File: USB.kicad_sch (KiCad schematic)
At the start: 91 parts, among them J1 USB_A, J2 USB-C Receptacle, J3 USB_A, J4 USB_A, J5 USB_A, U3 GL3523-OTY30, U4 USB-PD, U5 LPW5209AB5F, U6 LPW5209AB5F, U7 LPW5209AB5F, U8 LPW5209AB5F, U9 W25Q128JVS, Y1 Crystal 25MHz 2016

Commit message: initial routing
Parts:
- added C43: Cap 4.7uF 0402, Capacitor_SMD:C_0402_1005Metric, symbol Kalid:Cap 4.7uF 0402
- J1, J3, J4, J5: footprint Connector_USB:USB_A_Connfly_DS1095 -> Kalid:USB_A_Connfly_DS1095; LCSC (none) -> C456018; MPN (none) -> AF 90° WJDG; Manufacturer (none) -> SHOU HAN(首韩)
- J2: footprint Connector_USB:USB_C_Receptacle_HRO_TYPE-C-31-M-12 -> Kalid:USB_C_Receptacle_HRO_TYPE-C-31-M-12
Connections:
- net +1.2V: now also C21.1, C43.1
- net +V5V: no longer C21.1
- net GND: now also C43.2
- net USB_UFP_D+: no longer R42.2
- net USB_UFP_D-: no longer R43.2
- net P3_D-: now reaches J4.2 (D-), U3.14 (DM_P3)
- net P3_D+: now reaches J4.3 (D+), U3.13 (DP_P3)
- net at R40.1, U4.4 (D+): now also R43.1
- net at R41.1, U4.5 (D-): now also R42.1
- net P2_D+: now reaches J3.3 (D+), U3.25 (DP_P2)
- net P2_D-: now reaches J3.2 (D-), U3.26 (DM_P2)
- net P1_D-: now reaches J1.2 (D-), U3.64 (DM_P1)
- net P1_D+: now reaches J1.3 (D+), U3.63 (DP_P1)
- net P4_D+: now reaches J5.3 (D+), U3.10 (DP_P4)
- net P4_D-: now reaches J5.2 (D-), U3.11 (DM_P4)

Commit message: finish routing
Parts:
- added C44: Cap 4.7uF 0402, Capacitor_SMD:C_0402_1005Metric, symbol Kalid:Cap 4.7uF 0402
- added H1, H2, H3, H4: Mounting Hole, MountingHole:MountingHole_2.2mm_M2_DIN965_Pad_TopOnly, symbol Mechanical:MountingHole_Pad
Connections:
- net +1.2V: now also C44.1
- net +V5V: no longer C32.1, U4.2 (VUSB)
- net +VUSBIN: now also C32.1, U4.2 (VUSB)
- net GND: now also C44.2, H1.1, H2.1, H3.1, H4.1

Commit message: name the project
Signed-off-by: Sean Cross <sean@xobs.io>
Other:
- title: (none) -> Kalid
- moved on the sheet: H1, H2, H3, H4
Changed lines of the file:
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@@
 	(generator_version "9.0")
 	(paper "A4")
+	(title_block
+		(title "Kalid")
+		(date "2025-07-28")
+		(rev "EVT1")
+	)
 	(rectangle
 		(start 20.32 156.21)
@@
 	(symbol
 		(lib_id "Mechanical:MountingHole_Pad")
-		(at 142.24 106.68 0)
+		(at 130.81 85.09 0)
 		(unit 1)
 		(exclude_from_sim no)
@@
 		(fields_autoplaced yes)
 		(property "Reference" "H2"
-			(at 144.78 104.1399 0)
+			(at 133.35 82.5499 0)
 			(effects
 				(font
@@
 		)
 		(property "Value" "Mounting Hole"
-			(at 144.78 106.6799 0)
+			(at 133.35 85.0899 0)
 			(effects
 				(font
@@
 		)
 		(property "Footprint" "MountingHole:MountingHole_2.2mm_M2_DIN965_Pad_TopOnly"
-			(at 142.24 106.68 0)
+			(at 130.81 85.09 0)
 			(effects
 				(font
@@
 		)
 		(property "Datasheet" "~"
-			(at 142.24 106.68 0)
+			(at 130.81 85.09 0)
 			(effects
 				(font
@@
 		)
 		(property "Description" "Mounting Hole with connection"
-			(at 142.24 106.68 0)
+			(at 130.81 85.09 0)
 			(effects
 				(font
@@
 	(symbol
 		(lib_id "power:GND")
-		(at 121.92 109.22 0)
+		(at 110.49 87.63 0)
 		(unit 1)
 		(exclude_from_sim no)
@@
 		(fields_autoplaced yes)
 		(property "Reference" "#PWR086"
-			(at 121.92 115.57 0)
+			(at 110.49 93.98 0)
 			(effects
 				(font
@@
 		)
 		(property "Value" "GND"
-			(at 121.92 114.3 0)
+			(at 110.49 92.71 0)
 			(effects
 				(font
@@
 		)
 		(property "Footprint" ""
-			(at 121.92 109.22 0)
+			(at 110.49 87.63 0)
 			(effects
 				(font
@@
 		)
 		(property "Datasheet" ""
-			(at 121.92 109.22 0)
+			(at 110.49 87.63 0)
 			(effects
 				(font
@@
 		)
 		(property "Description" ""
-			(at 121.92 109.22 0)
+			(at 110.49 87.63 0)
 			(effects
 				(font
@@
 	(symbol
 		(lib_id "Mechanical:MountingHole_Pad")
-		(at 121.92 118.11 0)
+		(at 110.49 96.52 0)
 		(unit 1)
 		(exclude_from_sim no)
@@
 		(fields_autoplaced yes)
 		(property "Reference" "H3"
-			(at 124.46 115.5699 0)
+			(at 113.03 93.9799 0)
 			(effects
 				(font
@@
 		)
 		(property "Value" "Mounting Hole"
-			(at 124.46 118.1099 0)
+			(at 113.03 96.5199 0)
 			(effects
 				(font
@@
 		)
 		(property "Footprint" "MountingHole:MountingHole_2.2mm_M2_DIN965_Pad_TopOnly"
-			(at 121.92 118.11 0)
+			(at 110.49 96.52 0)
 			(effects
 				(font
@@
 		)
 		(property "Datasheet" "~"
-			(at 121.92 118.11 0)
+			(at 110.49 96.52 0)
 			(effects
 				(font
@@
 		)
 		(property "Description" "Mounting Hole with connection"
-			(at 121.92 118.11 0)
+			(at 110.49 96.52 0)
 			(effects
 				(font
@@
 	(symbol
 		(lib_id "Mechanical:MountingHole_Pad")
-		(at 142.24 118.11 0)
+		(at 130.81 96.52 0)
 		(unit 1)
 		(exclude_from_sim no)
@@
 		(fields_autoplaced yes)
 		(property "Reference" "H4"
-			(at 144.78 115.5699 0)
+			(at 133.35 93.9799 0)
 			(effects
 				(font
@@
 		)
 		(property "Value" "Mounting Hole"
-			(at 144.78 118.1099 0)
+			(at 133.35 96.5199 0)
 			(effects
 				(font
@@
 		)
 		(property "Footprint" "MountingHole:MountingHole_2.2mm_M2_DIN965_Pad_TopOnly"
-			(at 142.24 118.11 0)
+			(at 130.81 96.52 0)
 			(effects
 				(font
@@
 		)
 		(property "Datasheet" "~"
-			(at 142.24 118.11 0)
+			(at 130.81 96.52 0)
 			(effects
 				(font
@@
 		)
 		(property "Description" "Mounting Hole with connection"
-			(at 142.24 118.11 0)
+			(at 130.81 96.52 0)
 			(effects
 				(font
@@
 	(symbol
 		(lib_id "Mechanical:MountingHole_Pad")
-		(at 121.92 106.68 0)
+		(at 110.49 85.09 0)
 		(unit 1)
 		(exclude_from_sim no)
@@
 		(fields_autoplaced yes)
 		(property "Reference" "H1"
-			(at 124.46 104.1399 0)
+			(at 113.03 82.5499 0)
 			(effects
 				(font
@@
 		)
 		(property "Value" "Mounting Hole"
-			(at 124.46 106.6799 0)
+			(at 113.03 85.0899 0)
 			(effects
 				(font
@@
 		)
 		(property "Footprint" "MountingHole:MountingHole_2.2mm_M2_DIN965_Pad_TopOnly"
-			(at 121.92 106.68 0)
+			(at 110.49 85.09 0)
 			(effects
 				(font
@@
 		)
 		(property "Datasheet" "~"
-			(at 121.92 106.68 0)
+			(at 110.49 85.09 0)
 			(effects
 				(font
@@
 		)
 		(property "Description" "Mounting Hole with connection"
-			(at 121.92 106.68 0)
+			(at 110.49 85.09 0)
 			(effects
 				(font
@@
 	(symbol
 		(lib_id "power:GND")
-		(at 142.24 120.65 0)
+		(at 130.81 99.06 0)
 		(unit 1)
 		(exclude_from_sim no)
@@
 		(fields_autoplaced yes)
 		(property "Reference" "#PWR089"
-			(at 142.24 127 0)
+			(at 130.81 105.41 0)
 			(effects
 				(font
@@
 		)
 		(property "Value" "GND"
-			(at 142.24 125.73 0)
+			(at 130.81 104.14 0)
 			(effects
 				(font
@@
 		)
 		(property "Footprint" ""
-			(at 142.24 120.65 0)
+			(at 130.81 99.06 0)
 			(effects
 				(font
@@
 		)
 		(property "Datasheet" ""
-			(at 142.24 120.65 0)
+			(at 130.81 99.06 0)
 			(effects
 				(font
@@
 		)
 		(property "Description" ""
-			(at 142.24 120.65 0)
+			(at 130.81 99.06 0)
 			(effects
 				(font
@@
 	(symbol
 		(lib_id "power:GND")
-		(at 121.92 120.65 0)
+		(at 110.49 99.06 0)
 		(unit 1)
 		(exclude_from_sim no)
@@
 		(fields_autoplaced yes)
 		(property "Reference" "#PWR088"
-			(at 121.92 127 0)
+			(at 110.49 105.41 0)
 			(effects
 				(font
@@
 		)
 		(property "Value" "GND"
-			(at 121.92 125.73 0)
+			(at 110.49 104.14 0)
 			(effects
 				(font
@@
 		)
 		(property "Footprint" ""
-			(at 121.92 120.65 0)
+			(at 110.49 99.06 0)
 			(effects
 				(font
@@
 		)
 		(property "Datasheet" ""
-			(at 121.92 120.65 0)
+			(at 110.49 99.06 0)
 			(effects
 				(font
@@
 		)
 		(property "Description" ""
-			(at 121.92 120.65 0)
+			(at 110.49 99.06 0)
 			(effects
 				(font
@@
 	(symbol
 		(lib_id "power:GND")
-		(at 142.24 109.22 0)
+		(at 130.81 87.63 0)
 		(unit 1)
 		(exclude_from_sim no)
@@
 		(fields_autoplaced yes)
 		(property "Reference" "#PWR087"
-			(at 142.24 115.57 0)
+			(at 130.81 93.98 0)
 			(effects
 				(font
@@
 		)
 		(property "Value" "GND"
-			(at 142.24 114.3 0)
+			(at 130.81 92.71 0)
 			(effects
 				(font
@@
 		)
 		(property "Footprint" ""
-			(at 142.24 109.22 0)
+			(at 130.81 87.63 0)
 			(effects
 				(font
@@
 		)
 		(property "Datasheet" ""
-			(at 142.24 109.22 0)
+			(at 130.81 87.63 0)
 			(effects
 				(font
@@
 		)
 		(property "Description" ""
-			(at 142.24 109.22 0)
+			(at 130.81 87.63 0)
 			(effects
 				(font

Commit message: develop evt2
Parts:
- removed C17: Cap 4.7uF 0402, Capacitor_SMD:C_0402_1005Metric, symbol Kalid:Cap 4.7uF 0402
- removed L3: 10uH, 4.5A, Inductor_SMD:L_Changjiang_FXL0630, symbol Device:L
- removed R14, R15, R36: R 10k 0402, Resistor_SMD:R_0402_1005Metric, symbol Kalid:R 10k 0402
- removed R44, R45: R 0 ohm 0402, Resistor_SMD:R_0402_1005Metric, symbol Kalid:R 0 ohm 0402
- added L3: L 2.2uH 2A, Kalid:IND-SMD_L3.0-W3.0_LQH3NPN, symbol Kalid:L 2.2uH 2A
- added R14, R15: R 0 ohm 0402, Resistor_SMD:R_0402_1005Metric, symbol Kalid:R 0 ohm 0402
- added R36: R 5.1k 0402, Resistor_SMD:R_0402_1005Metric, symbol Kalid:R 5.1k 0402
- R39: now not fitted; now left out of the parts list
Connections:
- net +3.3V: now also R37.2, R38.2, R39.2, R14.2
- net +V5V: now also R15.2; no longer U3.54 (VBUS)
- net GND: now also R13.2; no longer R39.1
- net at U3.41 (SW): now also L3.2
- net at U3.45 (CHIPEN): now also R14.1, R15.1
- net at R38.1: now also U9.7 (~{HOLD}/~{RESET}/IO_{3}); no longer R39.2
- net at R12.1, U3.48 (RESETJ): now also R39.1; no longer R13.1
- net SPI_CS: now reaches U3.52 (P_SPI_CZ), U9.1 (~{CS})
- net SPI_CIPO: now reaches U9.2 (DO/IO_{1})
- net SPI_CIPO: now also U3.51 (P_SPI_DI); no longer U3.49 (P_SPI_DO)
- net at U9.3 (~{WP}/IO_{2}): now also R37.1
- net SPI_COPI: now reaches U9.5 (DI/IO_{0})
- net SPI_COPI: now also U3.49 (P_SPI_DO); no longer U3.51 (P_SPI_DI)
- net SPI_CLK: now reaches U3.50 (P_SPI_CK), U9.6 (CLK)
- net at R21.1: now also L3.1
- new net: R13.1, R36.1, U3.54 (VBUS)
- new net +V5VUSB: R36.2
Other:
- note removed: "10k on top, 50k on the bottom"
- moved on the sheet: C20, R12, R13

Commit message: evt3
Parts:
- removed C44: Cap 4.7uF 0402, Capacitor_SMD:C_0402_1005Metric, symbol Kalid:Cap 4.7uF 0402
- added C17: Cap 12pF 0402, Capacitor_SMD:C_0402_1005Metric, symbol Kalid:Cap 12pF 0402
- added FB1: 120 ohm, Inductor_SMD:L_0402_1005Metric, symbol Device:FerriteBead_Small
- added J6: Conn_01x04, Connector_PinSocket_2.54mm:PinSocket_1x04_P2.54mm_Vertical, symbol Connector_Generic:Conn_01x04
- added R44, R45, R58, R59, R60, R61, R62, R63: R 10k 0402, Resistor_SMD:R_0402_1005Metric, symbol Kalid:R 10k 0402
- added R64: R 0 ohm 0402, Resistor_SMD:R_0402_1005Metric, symbol Kalid:R 0 ohm 0402
- added TP11, TP8, TP9: TestPoint, TestPoint:TestPoint_Pad_D1.5mm, symbol Connector:TestPoint
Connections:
- net +1.2V: now also L3.1, R21.1, C17.2, FB1.1, TP9.1; no longer C27.1, C28.1, C30.1, C31.1, C38.1, R21.2, R22.1, U3.17 (VP12_P3), U3.22 (VP12_P2), U3.39 (FB), U3.60 (VP12_P1), U3.7 (VP12_P4), U3.70 (VP12_P0)
- net +3.3V: now also TP8.1
- net +V5V: now also R45.1, R59.1, R61.1, R63.1
- net GND: now also J6.1 (Pin_1), R44.2, R58.2, R60.2, R62.2, R64.2
- net SPI_CIPO: now also U3.49 (P_SPI_DO); no longer U3.51 (P_SPI_DI)
- net SPI_COPI: now also U3.51 (P_SPI_DI); no longer U3.49 (P_SPI_DO)
- net at TP4.1, U3.35 (OVCUR2J): now also R58.1, R59.2
- net SMD: now reaches TP6.1, U3.31 (OVCUR4J/SMD)
- net SMD: now also J6.3 (Pin_3), R62.1, R63.2
- net SMC: now reaches TP5.1, U3.34 (OVCUR3J/SMC)
- net SMC: now also J6.2 (Pin_2), R60.1, R61.2
- net RESETJ: now reaches R12.1, R39.1, U3.48 (RESETJ)
- net RESETJ: now also J6.4 (Pin_4), R64.1
- net at TP3.1, U3.38 (OVCUR1J): now also R44.1, R45.2
- new net: C17.1, R21.2, R22.1, U3.39 (FB)
- new net +1.2VP: C27.1, C28.1, C30.1, C31.1, C38.1, FB1.2, TP11.1, U3.17 (VP12_P3), U3.22 (VP12_P2), U3.60 (VP12_P1), U3.7 (VP12_P4), U3.70 (VP12_P0)
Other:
- moved on the sheet: C21, C27, C28, C30, C31, C38, C43, L3, R12, R21, R39

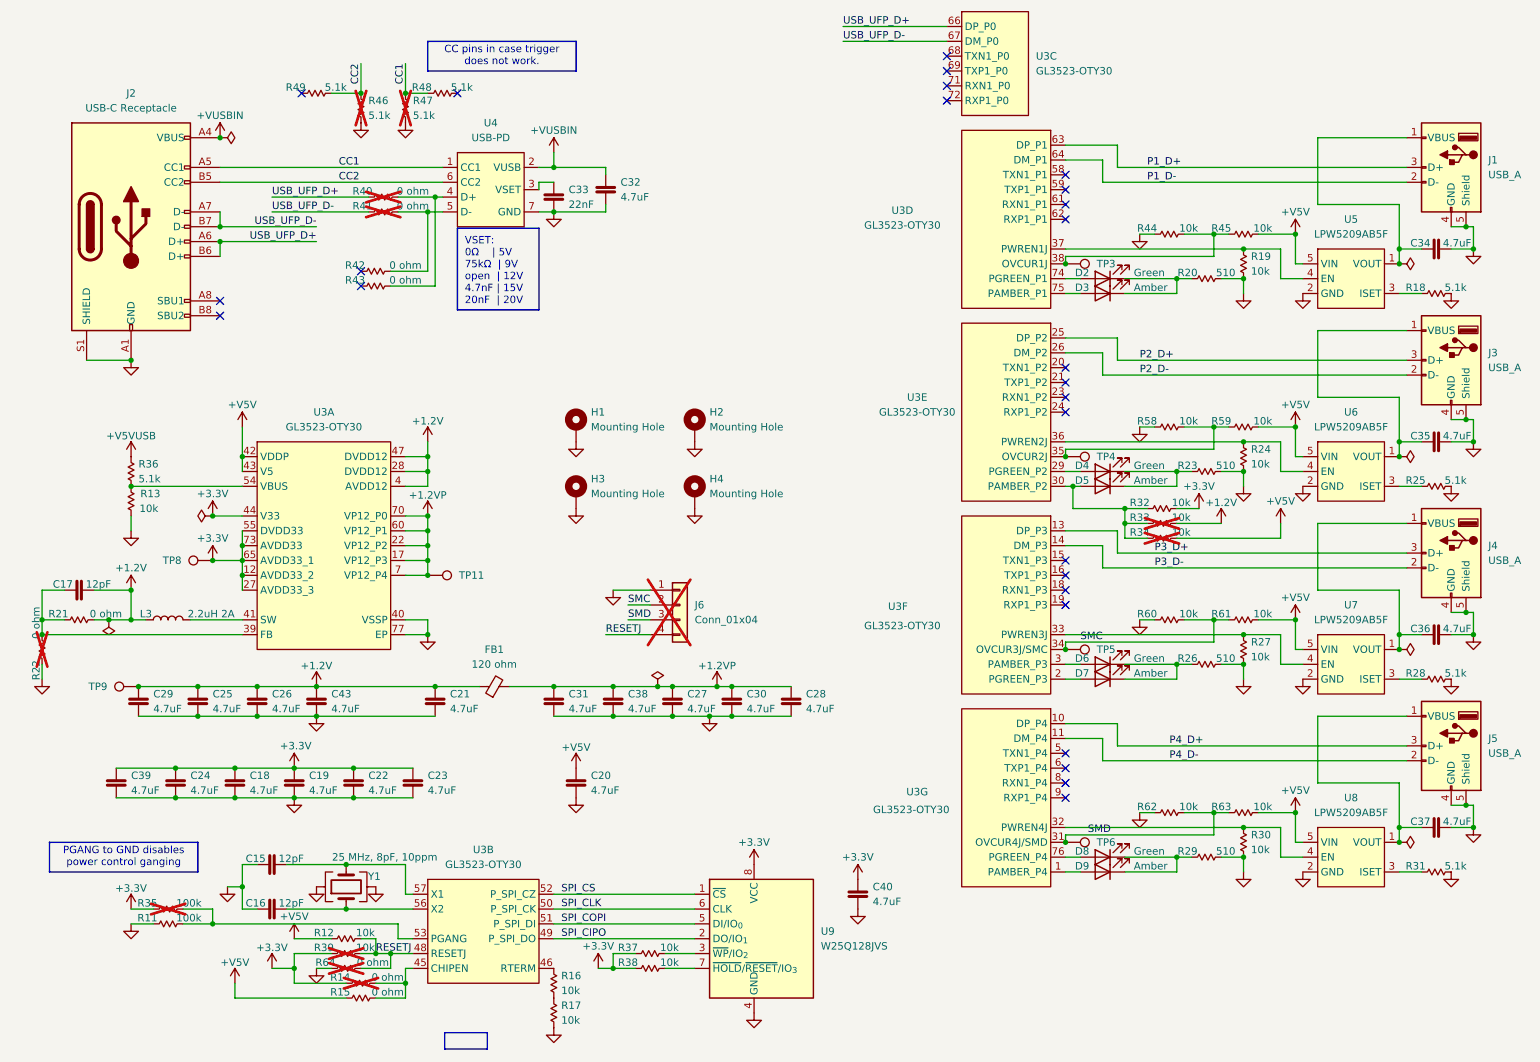
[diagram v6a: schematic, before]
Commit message: evt4 - route usb3 lines
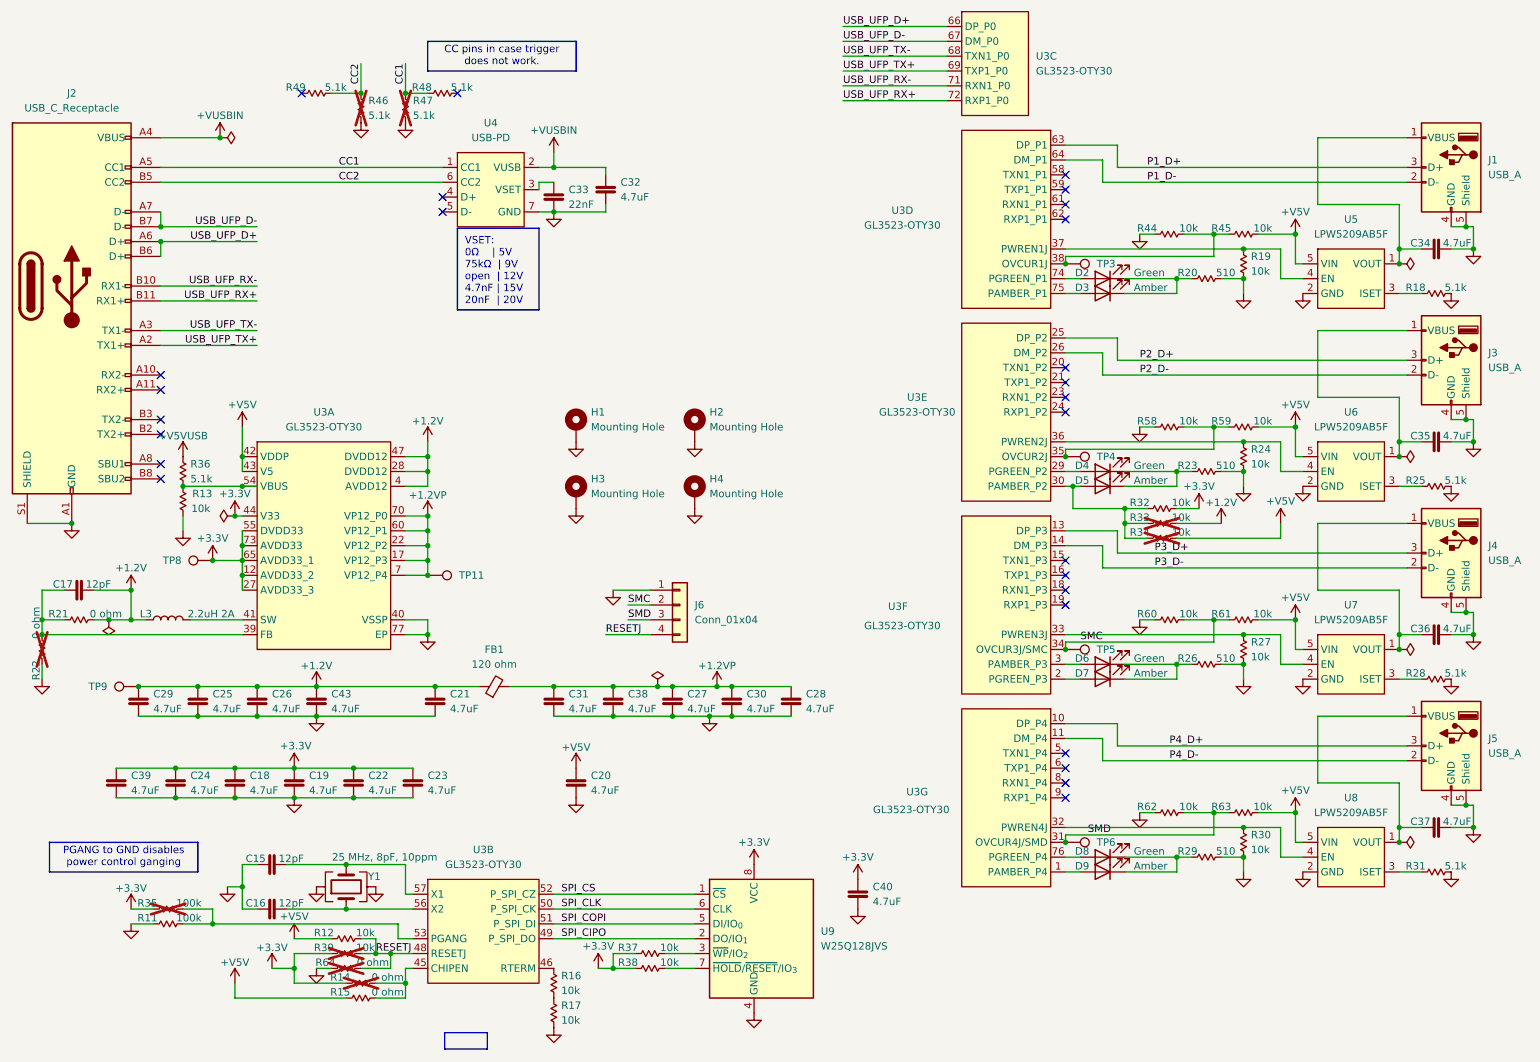
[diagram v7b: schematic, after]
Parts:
- removed J2: USB-C Receptacle, Kalid:USB_C_Receptacle_HRO_TYPE-C-31-M-12, symbol Connector:USB_C_Receptacle_USB2.0_16P
- removed R40, R41, R42, R43: R 0 ohm 0402, Resistor_SMD:R_0402_1005Metric, symbol Kalid:R 0 ohm 0402
- added J2: USB_C_Receptacle, Kalid:USB-C-SMD_TYPE-C-24P-QT, symbol Connector:USB_C_Receptacle
- J6: footprint Connector_PinSocket_2.54mm:PinSocket_1x04_P2.54mm_Vertical -> Connector_PinHeader_2.54mm:PinHeader_1x04_P2.54mm_Vertical; LCSC (none) -> C2691448; MPN (none) -> PZ254V-11-04P; Manufacturer (none) -> XFCN; now fitted
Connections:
- net +VUSBIN: now also J2.A4 (VBUS), J2.A9 (VBUS), J2.B4 (VBUS), J2.B9 (VBUS)
- net CC1: now also J2.A5 (CC1)
- net CC2: now also J2.B5 (CC2)
- net GND: now also J2.A1 (GND), J2.A12 (GND), J2.B1 (GND), J2.B12 (GND), J2.S1 (SHIELD)
- net USB_UFP_D+: now also J2.A6 (D+), J2.B6 (D+)
- net USB_UFP_D-: now also J2.A7 (D-), J2.B7 (D-)
- net USB_UFP_TX-: now reaches U3.68 (TXN1_P0)
- net USB_UFP_TX-: now also J2.A3 (TX1-)
- net USB_UFP_TX+: now reaches U3.69 (TXP1_P0)
- net USB_UFP_TX+: now also J2.A2 (TX1+)
- net USB_UFP_RX-: now reaches U3.71 (RXN1_P0)
- net USB_UFP_RX-: now also J2.B10 (RX1-)
- net USB_UFP_RX+: now reaches U3.72 (RXP1_P0)
- net USB_UFP_RX+: now also J2.B11 (RX1+)
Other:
- moved on the sheet: R13, R36

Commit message: release evt5
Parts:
- removed J2: USB_C_Receptacle, Kalid:USB-C-SMD_TYPE-C-24P-QT, symbol Connector:USB_C_Receptacle
- removed R46, R47, R48, R49: R 5.1k 0402, Resistor_SMD:R_0402_1005Metric, symbol Kalid:R 5.1k 0402
- added C44, C45, C46, C47: Cap 22uF, Capacitor_SMD:C_0805_2012Metric, symbol Kalid:Cap 22uF 0805
- added J7: USB_C_Receptacle_USB2.0_16P, Kalid:USB_C_Receptacle_HRO_TYPE-C-31-M-12, symbol Connector:USB_C_Receptacle_USB2.0_16P
- added R40: R 1M 0402, Resistor_SMD:R_0402_1005Metric, symbol Kalid:R 1M 0402
- added R41, R42, R43, R46: R 0 ohm 0402, Resistor_SMD:R_0402_1005Metric, symbol Kalid:R 0 ohm 0402
- U9: value W25Q128JVS -> MX25L1006EMI-10G; LCSC C97521 -> C71944; MPN W25Q128JVSIQ -> MX25L1006EMI-10G; Manufacturer Winbond Elec -> MXIC(Macronix)
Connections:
- net +1.2V: now also C44.1, C45.1
- net +3.3V: now also C46.1, C47.1
- net +VUSBIN: now also J7.A4 (VBUS), J7.A9 (VBUS), J7.B4 (VBUS), J7.B9 (VBUS)
- net CC1: now also J7.A5 (CC1)
- net CC2: now also J7.B5 (CC2)
- net GND: now also C44.2, C45.2, C46.2, C47.2, J7.A1 (GND), J7.A12 (GND), J7.B1 (GND), J7.B12 (GND), J7.S1 (SHIELD)
- net SPI_CIPO: now also R42.1, R43.1; no longer U3.49 (P_SPI_DO)
- net SPI_COPI: now also R41.1, R46.1; no longer U3.51 (P_SPI_DI)
- net USB_UFP_D+: now also J7.A6 (D+), J7.B6 (D+)
- net USB_UFP_D-: now also J7.A7 (D-), J7.B7 (D-)
- net at C16.2, U3.56 (X2), Y1.1: now also R40.1
- net at C15.2, U3.57 (X1), Y1.3: now also R40.2
- net USB_UFP_RX+: no longer names the net of U3.72 (RXP1_P0)
- net USB_UFP_RX-: no longer names the net of U3.71 (RXN1_P0)
- net USB_UFP_TX+: no longer names the net of U3.69 (TXP1_P0)
- net USB_UFP_TX-: no longer names the net of U3.68 (TXN1_P0)
- new net: R42.2, R46.2, U3.51 (P_SPI_DI)
- new net: R41.2, R43.2, U3.49 (P_SPI_DO)
- no-connect marks 26 -> 24
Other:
- note removed: "CC pins in case trigger does not work."
- moved on the sheet: C15, C16, C20, C21, C25, C26, C27, C28, C29, C30, C31, C32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
